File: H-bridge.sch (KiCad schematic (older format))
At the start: 15 parts

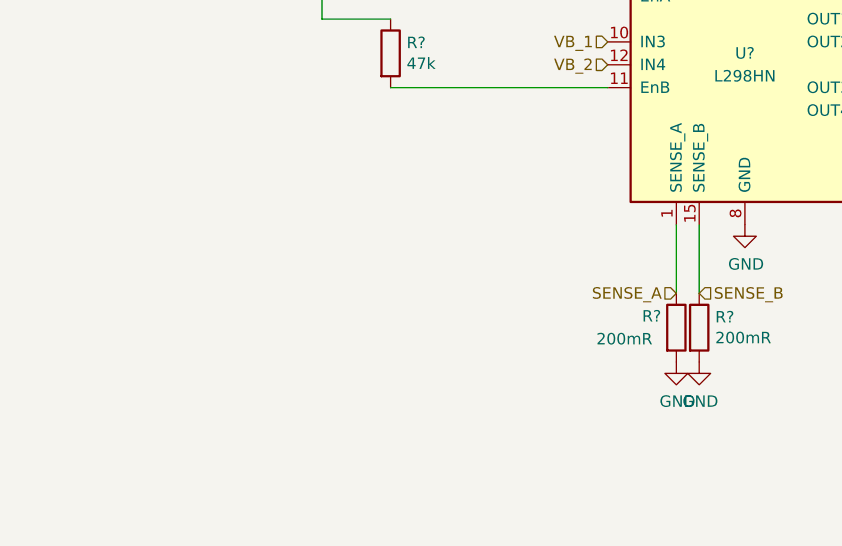
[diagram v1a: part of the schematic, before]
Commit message: Added housekeeping ADC, schematics almost done
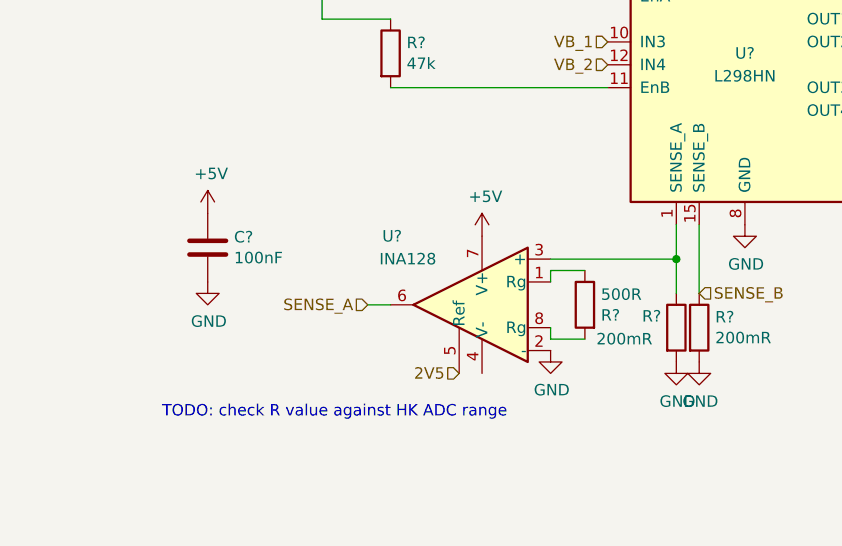
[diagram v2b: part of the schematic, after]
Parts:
- added C?: 100nF, symbol Device:C
- added R?: 500R, symbol Device:R
- added U?: INA128, symbol Amplifier_Instrumentation:INA128
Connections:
- net +5V: now also C?.1, U?.7 (V+)
- net GND: now also C?.2, U?.2 (-)
- net SENSE_A: now also U?.6; no longer R?.1, U?.1 (SENSE_A)
- new net: R?.1, U?.1 (SENSE_A), U?.3 (+)
- new net: R?.1, U?.1 (Rg)
- new net: R?.2, U?.8 (Rg)
- new net 2V5: U?.5 (Ref)
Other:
- note added: "TODO: check R value against HK ADC range"
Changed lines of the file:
@@
 Not sure if there is a better way to label the IN 1,2,3,4 \n
 Wire Wire Line
-	5350 4200 5350 4500
+	5350 4200 5350 4350
 Text HLabel 5450 4500 2    50   Input ~ 0
 SENSE_B
-Text HLabel 5350 4500 0    50   Input ~ 0
+Text HLabel 4000 4550 0    50   Input ~ 0
 SENSE_A
 Wire Wire Line
@@
 	1    0    0    -1
 $EndComp
+Text Notes 3100 5050 0    50   ~ 0
+TODO: check R value against HK ADC range
+$Comp
+L Amplifier_Instrumentation:INA128 U?
+U 1 1 5C4B5673
+P 4500 4550
+F 0 "U?" H 4850 4850 50  0000 L CNN
+F 1 "INA128" H 4700 4750 50  0000 L CNN
+F 2 "" H 4600 4550 50  0001 C CNN
+F 3 "http://www.ti.com/lit/ds/symlink/ina128.pdf" H 4600 4550 50  0001 C CNN
+	1    4500 4550
+	-1   0    0    -1
+$EndComp
+$Comp
+L Device:R R?
+U 1 1 5C4B589F
+P 4950 4550
+F 0 "R?" H 4880 4504 50  0000 R CNN
+F 1 "500R" H 4880 4595 50  0000 R CNN
+F 2 "" V 4880 4550 50  0001 C CNN
+F 3 "~" H 4950 4550 50  0001 C CNN
+	1    4950 4550
+	-1   0    0    -1
+$EndComp
+Wire Wire Line
+	4950 4700 4800 4700
+Wire Wire Line
+	4800 4700 4800 4650
+Wire Wire Line
+	4800 4450 4800 4400
+Wire Wire Line
+	4800 4400 4950 4400
+Wire Wire Line
+	4000 4550 4100 4550
+$Comp
+L power:+5V #PWR?
+U 1 1 5C4B6CBA
+P 4500 4250
+F 0 "#PWR?" H 4500 4100 50  0001 C CNN
+F 1 "+5V" H 4515 4423 50  0000 C CNN
+F 2 "" H 4500 4250 50  0001 C CNN
+F 3 "" H 4500 4250 50  0001 C CNN
+	1    4500 4250
+	1    0    0    -1
+$EndComp
+$Comp
+L power:+5V #PWR?
+U 1 1 5C4B6CEE
+P 3300 4150
+F 0 "#PWR?" H 3300 4000 50  0001 C CNN
+F 1 "+5V" H 3315 4323 50  0000 C CNN
+F 2 "" H 3300 4150 50  0001 C CNN
+F 3 "" H 3300 4150 50  0001 C CNN
+	1    3300 4150
+	1    0    0    -1
+$EndComp
+$Comp
+L Device:C C?
+U 1 1 5C4B6D58
+P 3300 4300
+F 0 "C?" H 3415 4346 50  0000 L CNN
+F 1 "100nF" H 3415 4255 50  0000 L CNN
+F 2 "" H 3338 4150 50  0001 C CNN
+F 3 "~" H 3300 4300 50  0001 C CNN
+	1    3300 4300
+	1    0    0    -1
+$EndComp
+$Comp
+L power:GND #PWR?
+U 1 1 5C4B6E7F
+P 3300 4450
+F 0 "#PWR?" H 3300 4200 50  0001 C CNN
+F 1 "GND" H 3305 4277 50  0000 C CNN
+F 2 "" H 3300 4450 50  0001 C CNN
+F 3 "" H 3300 4450 50  0001 C CNN
+	1    3300 4450
+	1    0    0    -1
+$EndComp
+Text HLabel 4400 4850 0    50   Input ~ 0
+2V5
+Wire Wire Line
+	4800 4350 5350 4350
+Connection ~ 5350 4350
+Wire Wire Line
+	5350 4350 5350 4500
+$Comp
+L power:GND #PWR?
+U 1 1 5C4B7865
+P 4800 4750
+AR Path="/5C4B7865" Ref="#PWR?"  Part="1"
+AR Path="/5BE41DDF/5C4B7865" Ref="#PWR?"  Part="1"
+AR Path="/5BE443F5/5C4B7865" Ref="#PWR?"  Part="1"
+AR Path="/5BEEC4C8/5C4B7865" Ref="#PWR?"  Part="1"
+AR Path="/5BEEC636/5C4B7865" Ref="#PWR?"  Part="1"
+F 0 "#PWR?" H 4800 4500 50  0001 C CNN
+F 1 "GND" H 4805 4577 50  0000 C CNN
+F 2 "" H 4800 4750 50  0001 C CNN
+F 3 "" H 4800 4750 50  0001 C CNN
+	1    4800 4750
+	1    0    0    -1
+$EndComp

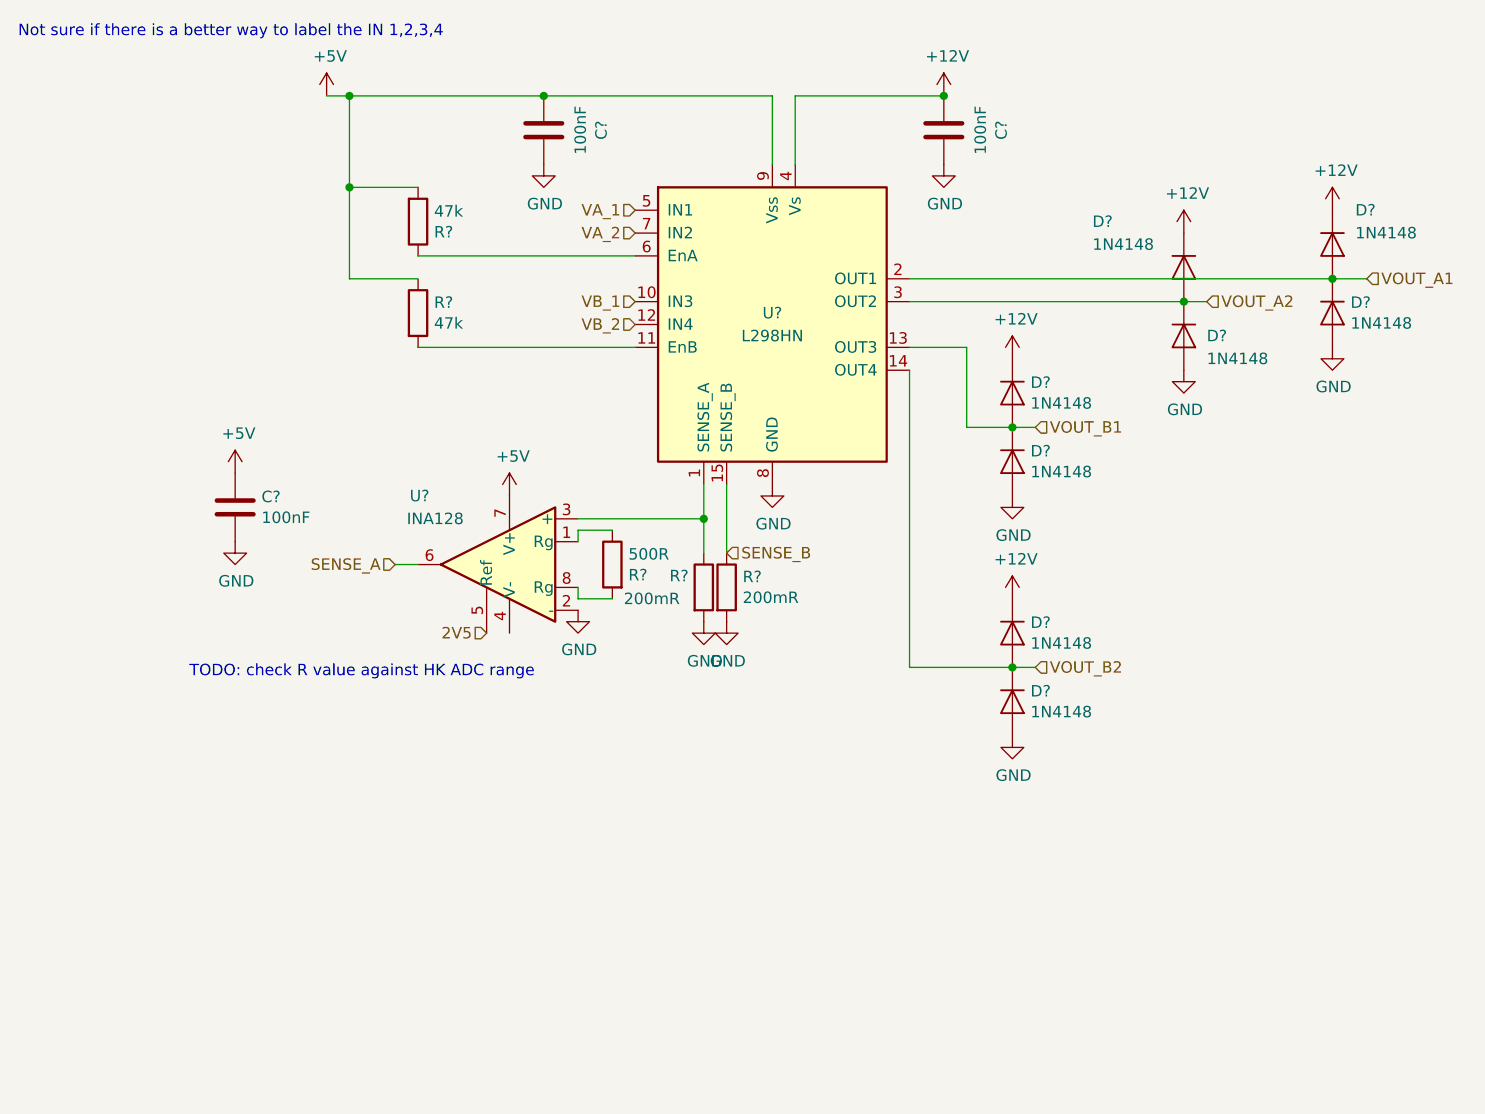
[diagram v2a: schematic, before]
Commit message: Schematics Done. Now need to do footprints
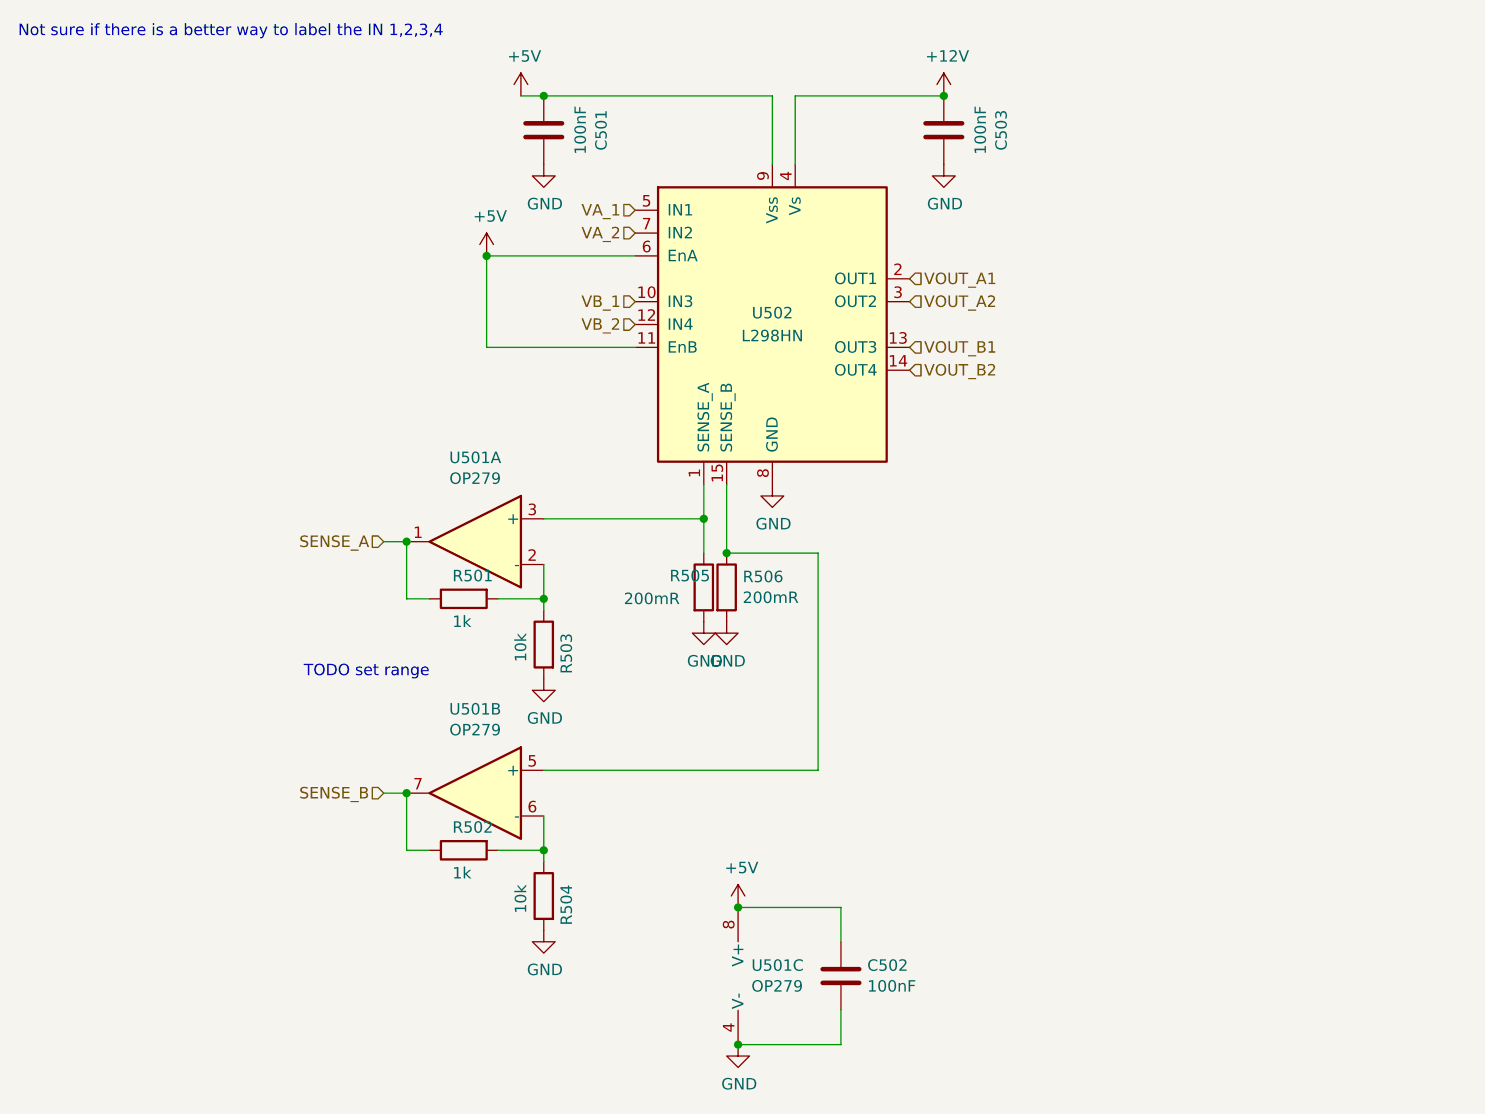
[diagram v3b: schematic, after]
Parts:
- removed D? (x8): 1N4148, Diode_THT:D_DO-35_SOD27_P7.62mm_Horizontal, symbol Diode:1N4148
- removed R? (x2): 47k, symbol Device:R
- removed U?: INA128, symbol Amplifier_Instrumentation:INA128
- added R202: 1k, Resistor_SMD:R_0805_2012Metric, symbol Device:R
- added R203, R204: 10k, Resistor_SMD:R_0805_2012Metric, symbol Device:R
- added U401: OP279, symbol Amplifier_Operational:OP279
- R201: renamed from R?; value 500R -> 1k; footprint (none) -> Resistor_SMD:R_0805_2012Metric
- R205, R206: renamed from R?; footprint (none) -> Resistor_SMD:R_0805_2012Metric
- gave numbers to parts that had none: 4
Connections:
- net +5V: now also U202.11 (EnB), U202.6 (EnA), U401.8 (V+)
- net GND: now also R203.2, R204.2, U401.4 (V-)
- net SENSE_A: now also R201.1, U401.1
- net SENSE_B: now also R202.1, U401.7; no longer R206.1, U202.15 (SENSE_B)
- net at R205.1, U202.1 (SENSE_A): now also U401.3 (+)
- net at R201.2: now also R203.1, U401.2 (-)
- new net: R206.1, U202.15 (SENSE_B), U401.5 (+)
- new net: R202.2, R204.1, U401.6 (-)
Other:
- note added: "TODO set range"
- note removed: "TODO: check R value against HK ADC range"
- moved on the sheet: C502, R501

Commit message: Schematics done, now assigning footprints to do PCB Next
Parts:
- C201, C202, C203: footprint (none) -> Capacitor_SMD:C_0805_2012Metric
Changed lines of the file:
@@
 AR Path="/5BEEC4C8/5BE42F54" Ref="U402"  Part="1"
 AR Path="/5BEEC636/5BE42F54" Ref="U502"  Part="1"
-F 0 "U502" H 5650 3550 50  0000 C CNN
+F 0 "U202" H 5650 3550 50  0000 C CNN
 F 1 "L298HN" H 5650 3450 50  0000 C CNN
 F 2 "Package_TO_SOT_THT:TO-220-15_P2.54x2.54mm_StaggerOdd_Lead4.58mm_Vertical" H 5700 2850 50  0001 L CNN
@@
 AR Path="/5BEEC4C8/5BE42F71" Ref="R406"  Part="1"
 AR Path="/5BEEC636/5BE42F71" Ref="R506"  Part="1"
-F 0 "R506" H 5520 4696 50  0000 L CNN
+F 0 "R206" H 5520 4696 50  0000 L CNN
 F 1 "200mR" H 5520 4605 50  0000 L CNN
 F 2 "Resistor_SMD:R_0805_2012Metric" V 5380 4650 50  0001 C CNN
@@
 AR Path="/5BEEC4C8/5BE42F8D" Ref="C401"  Part="1"
 AR Path="/5BEEC636/5BE42F8D" Ref="C501"  Part="1"
-F 0 "C501" V 4398 2650 50  0000 C CNN
+F 0 "C201" V 4398 2650 50  0000 C CNN
 F 1 "100nF" V 4489 2650 50  0000 C CNN
-F 2 "" H 4688 2500 50  0001 C CNN
+F 2 "Capacitor_SMD:C_0805_2012Metric" H 4688 2500 50  0001 C CNN
 F 3 "~" H 4650 2650 50  0001 C CNN
 	1    4650 2650
@@
 AR Path="/5BEEC4C8/5BE42F94" Ref="C403"  Part="1"
 AR Path="/5BEEC636/5BE42F94" Ref="C503"  Part="1"
-F 0 "C503" V 6148 2650 50  0000 C CNN
+F 0 "C203" V 6148 2650 50  0000 C CNN
 F 1 "100nF" V 6239 2650 50  0000 C CNN
-F 2 "" H 6438 2500 50  0001 C CNN
+F 2 "Capacitor_SMD:C_0805_2012Metric" H 6438 2500 50  0001 C CNN
 F 3 "~" H 6400 2650 50  0001 C CNN
 	1    6400 2650
@@
 AR Path="/5BEEC4C8/5BE4772A" Ref="R405"  Part="1"
 AR Path="/5BEEC636/5BE4772A" Ref="R505"  Part="1"
-F 0 "R505" H 5200 4700 50  0000 L CNN
+F 0 "R205" H 5200 4700 50  0000 L CNN
 F 1 "200mR" H 5000 4600 50  0000 L CNN
 F 2 "Resistor_SMD:R_0805_2012Metric" V 5280 4650 50  0001 C CNN
@@
 AR Path="/5BEEC4C8/5C4B589F" Ref="R401"  Part="1"
 AR Path="/5BEEC636/5C4B589F" Ref="R501"  Part="1"
-F 0 "R501" V 4200 4750 50  0000 R CNN
+F 0 "R201" V 4200 4750 50  0000 R CNN
 F 1 "1k" V 4400 4750 50  0000 R CNN
 F 2 "Resistor_SMD:R_0805_2012Metric" V 4230 4700 50  0001 C CNN
@@
 AR Path="/5BEEC4C8/5C4B6D58" Ref="C402"  Part="1"
 AR Path="/5BEEC636/5C4B6D58" Ref="C502"  Part="1"
-F 0 "C502" H 6065 6396 50  0000 L CNN
+F 0 "C202" H 6065 6396 50  0000 L CNN
 F 1 "100nF" H 6065 6305 50  0000 L CNN
-F 2 "" H 5988 6200 50  0001 C CNN
+F 2 "Capacitor_SMD:C_0805_2012Metric" H 5988 6200 50  0001 C CNN
 F 3 "~" H 5950 6350 50  0001 C CNN
 	1    5950 6350
@@
 AR Path="/5BEEC636/5C5CDC2F" Ref="U501"  Part="1"
 AR Path="/5BE41DDF/5C5CDC2F" Ref="U201"  Part="1"
-F 0 "U501" H 4350 4817 50  0000 C CNN
+F 0 "U201" H 4350 4817 50  0000 C CNN
 F 1 "OP279" H 4350 4726 50  0000 C CNN
 F 2 "" H 4350 4450 50  0001 C CNN
@@
 AR Path="/5BEEC636/5C5CE16B" Ref="U501"  Part="2"
 AR Path="/5BE41DDF/5C5CE16B" Ref="U201"  Part="2"
-F 0 "U501" H 4350 5917 50  0000 C CNN
+F 0 "U201" H 4350 5917 50  0000 C CNN
 F 1 "OP279" H 4350 5826 50  0000 C CNN
 F 2 "" H 4350 5550 50  0001 C CNN
@@
 AR Path="/5BEEC636/5C5CE212" Ref="U501"  Part="3"
 AR Path="/5BE41DDF/5C5CE212" Ref="U201"  Part="3"
-F 0 "U501" H 5558 6396 50  0000 L CNN
+F 0 "U201" H 5558 6396 50  0000 L CNN
 F 1 "OP279" H 5558 6305 50  0000 L CNN
 F 2 "" H 5600 6350 50  0001 C CNN
@@
 AR Path="/5BEEC4C8/5C5D032D" Ref="R403"  Part="1"
 AR Path="/5BEEC636/5C5D032D" Ref="R503"  Part="1"
-F 0 "R503" V 4550 4950 50  0000 R CNN
+F 0 "R203" V 4550 4950 50  0000 R CNN
 F 1 "10k" V 4750 4950 50  0000 R CNN
 F 2 "Resistor_SMD:R_0805_2012Metric" V 4580 4900 50  0001 C CNN
@@
 AR Path="/5BEEC4C8/5C5D589D" Ref="R402"  Part="1"
 AR Path="/5BEEC636/5C5D589D" Ref="R502"  Part="1"
-F 0 "R502" V 4200 5850 50  0000 R CNN
+F 0 "R202" V 4200 5850 50  0000 R CNN
 F 1 "1k" V 4400 5850 50  0000 R CNN
 F 2 "Resistor_SMD:R_0805_2012Metric" V 4230 5800 50  0001 C CNN
@@
 AR Path="/5BEEC4C8/5C5D58B3" Ref="R404"  Part="1"
 AR Path="/5BEEC636/5C5D58B3" Ref="R504"  Part="1"
-F 0 "R504" V 4550 6050 50  0000 R CNN
+F 0 "R204" V 4550 6050 50  0000 R CNN
 F 1 "10k" V 4750 6050 50  0000 R CNN
 F 2 "Resistor_SMD:R_0805_2012Metric" V 4580 6000 50  0001 C CNN
